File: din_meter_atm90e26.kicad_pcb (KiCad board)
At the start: 2 copper layers, 32 x 31.1 mm, 61 parts, among them J1 USEL, J2 MMD1, J3 MMD0, J4 CONN_02X18, J5 CONN_01X10, J6 USEL, J7 MMD1, J8 MMD0, M1 ATM90E26_ATM90E26, M2 ATM90E26_ATM90E26, Y1 Crystal_Small, Y2 Crystal_Small

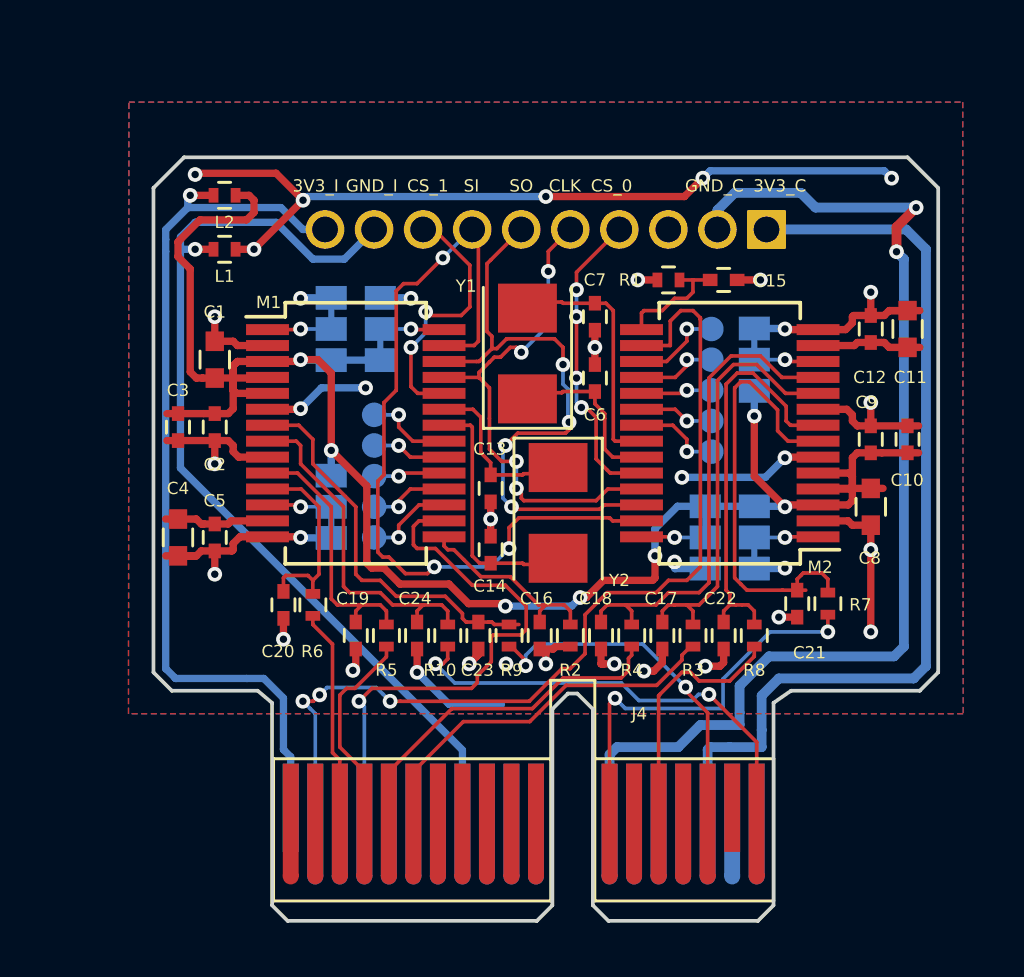
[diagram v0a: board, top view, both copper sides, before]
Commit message: First pass at layout.
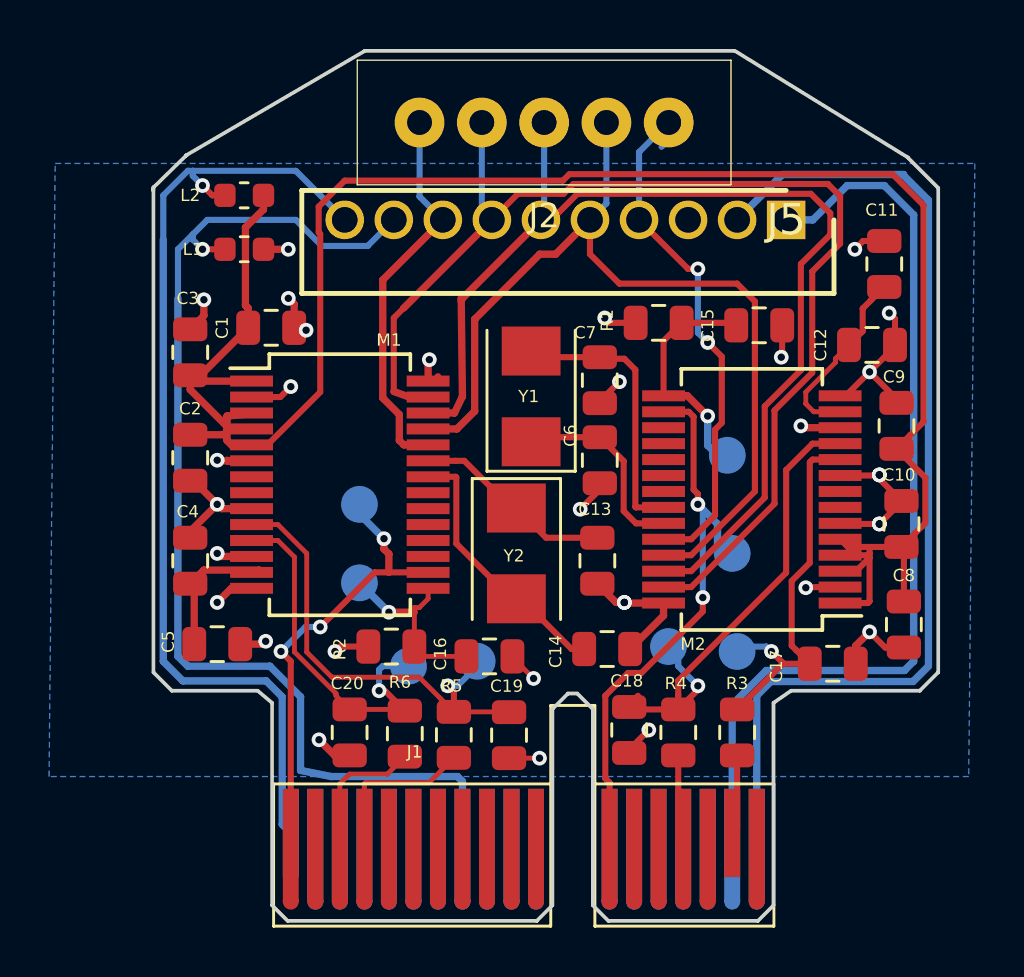
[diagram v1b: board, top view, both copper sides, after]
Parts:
- removed C21, C22, C23, C24: 33n, Capacitors_SMD:C_0402
- removed CF1_0: CF1_0, Measurement_Points:Measurement_Point_Round-SMD-Pad_Small
- removed CF1_1: CF1_1, Measurement_Points:Measurement_Point_Round-SMD-Pad_Small
- removed CF2_0: CF2_0, Measurement_Points:Measurement_Point_Round-SMD-Pad_Small
- removed CF2_1: CF2_1, Measurement_Points:Measurement_Point_Round-SMD-Pad_Small
- removed IRQ_0: IRQ_0, Measurement_Points:Measurement_Point_Round-SMD-Pad_Small
- removed IRQ_1: IRQ_1, Measurement_Points:Measurement_Point_Round-SMD-Pad_Small
- removed J3, J8: MMD0, Connectors:GS3
- removed J4: CONN_02X18, Connectors:PCI-EXPRESS
- removed J6: USEL, Connectors:GS3
- removed J7: MMD1, Connectors:GS3
- removed LOGO1: Logo_Open_Hardware_Small, Symbols:OSHW-Logo2_7.3x6mm_SilkScreen
- removed R10, R7, R8, R9: 1K, Resistors_SMD:R_0402
- removed WARN_0: WARN_0, Measurement_Points:Measurement_Point_Round-SMD-Pad_Small
- removed WARN_1: WARN_1, Measurement_Points:Measurement_Point_Round-SMD-Pad_Small
- removed ZX_0: ZX_0, Measurement_Points:Measurement_Point_Round-SMD-Pad_Small
- removed ZX_1: ZX_1, Measurement_Points:Measurement_Point_Round-SMD-Pad_Small
- added TP_I1N_0: I1N_0, MeasurementPoints:Measurement_Point_Round-SMD-Pad_Small, B.Cu at (150.9, 78.3)
- added TP_I1N_1: I1N_1, MeasurementPoints:Measurement_Point_Round-SMD-Pad_Small, B.Cu at (140.3, 79.2)
- added TP_I1P_0: I1P_0, MeasurementPoints:Measurement_Point_Round-SMD-Pad_Small, B.Cu at (153.7, 78.5)
- added TP_I1P_1: I1P_1, MeasurementPoints:Measurement_Point_Round-SMD-Pad_Small, B.Cu at (143.1, 79.0)
- added TP_VN_0: VN_0, MeasurementPoints:Measurement_Point_Round-SMD-Pad_Small, B.Cu at (153.3, 70.5)
- added TP_VN_1: VN_1, MeasurementPoints:Measurement_Point_Round-SMD-Pad_Small, B.Cu at (138.3, 75.8)
- added TP_VP_0: VP_0, MeasurementPoints:Measurement_Point_Round-SMD-Pad_Small, B.Cu at (153.5, 74.5)
- added TP_VP_1: VP_1, MeasurementPoints:Measurement_Point_Round-SMD-Pad_Small, B.Cu at (138.3, 72.5)
- C1, C11, C4, C8: footprint Capacitors_SMD:C_0603 -> Capacitor_SMD:C_0805_2012Metric
- C10, C12, C2, C3, C5, C9: value 100n -> .1u; footprint Capacitors_SMD:C_0402 -> Capacitor_SMD:C_0805_2012Metric
- C13, C14, C6, C7: footprint Capacitors_SMD:C_0402 -> Capacitor_SMD:C_0805_2012Metric
- C15, C16, C17, C18, C19, C20: value 33n -> .033u; footprint Capacitors_SMD:C_0402 -> Capacitor_SMD:C_0805_2012Metric
- J1: value USEL -> PCIx1; footprint Connectors:GS3 -> Connectors:PCI-EXPRESS; moved to F.Cu
- J2: value MMD1 -> Conn_01x05; footprint Connectors:GS3 -> FitHome_conn:conn_5_2.54mm; moved to F.Cu
- J5: moved to F.Cu
- L1, L2: footprint Inductors_SMD:L_0402 -> Inductor_SMD:L_0603_1608Metric
- M1, M2: footprint Housings_SSOP:SSOP-28_5.3x10.2mm_Pitch0.65mm -> Housings:SSOP-28_5.3x10.2mm_Pitch0.65mm
- R1, R2, R3, R4, R5, R6: footprint Resistors_SMD:R_0402 -> Resistor_SMD:R_0805_2012Metric
- Y1, Y2: footprint Crystals:Crystal_SMD_5032-2pin_5.0x3.2mm -> Crystal:Crystal_SMD_5032-2Pin_5.0x3.2mm
- moved SYM1 19.4 mm to (139.3, 67.0), turned to 180 degrees
- moved G1 16.6 mm to (152.7, 66.9)
- moved J1 13.4 mm to (135.5, 86.0)
- moved J2 9.16 mm to (140.8, 57.0), turned to 0 degrees
- moved C19 7.45 mm to (144.4, 82.0)
- moved R2 7.31 mm to (139.6, 78.3), turned to 180 degrees
- moved C17 7.04 mm to (157.6, 79.0), turned to 180 degrees
- moved R6 6.45 mm to (140.2, 81.9)
- moved C14 6.24 mm to (148.4, 78.5), turned to 180 degrees
- moved C20 5.86 mm to (137.9, 81.8)
- moved C13 5.26 mm to (148.0, 74.8)
- moved C8 4.99 mm to (160.5, 77.5)
- moved R5 4.90 mm to (142.2, 82.0)
- moved R4 4.38 mm to (151.3, 81.8)
- moved C5 4.35 mm to (132.5, 78.2), turned to 0 degrees
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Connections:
- J2 pad 1: GNDD -> CS_1
- J2 pad 2: Net-(J2-Pad2) -> MOSI_M
- J2 pad 3: +3V3 -> MISO_M
- J5 pad 10: 3V3_ISO -> 3V3_M
- J5 pad 5: SCLK -> SCLK_M
- J5 pad 6: SO/TX -> MISO_M
- J5 pad 7: SI/RX -> MOSI_M
- J5 pad 9: GND_ISO -> GND_M
- L1 pad 1: GND_ISO -> GND_M
- L2 pad 1: 3V3_ISO -> 3V3_M
- M1 pad 1: Net-(J2-Pad2) -> +3V3
- M1 pad 12: Net-(J1-Pad2) -> GNDD
- M1 pad 25: SCLK -> SCLK_M
- M1 pad 26: SO/TX -> MISO_M
- M1 pad 27: SI/RX -> MOSI_M
- M1 pad 28: Net-(J3-Pad2) -> GNDD
- M1 pad 7: I2P_1 -> Net-(M1-Pad7)
- M1 pad 8: I2N_1 -> Net-(M1-Pad8)
- M2 pad 1: Net-(J7-Pad2) -> +3V3
- M2 pad 12: Net-(J6-Pad2) -> GNDD
- M2 pad 25: SCLK -> SCLK_M
- M2 pad 26: SO/TX -> MISO_M
- M2 pad 27: SI/RX -> MOSI_M
- M2 pad 28: Net-(J8-Pad2) -> GNDD
- M2 pad 7: I2P_0 -> Net-(M2-Pad7)
- M2 pad 8: I2N_0 -> Net-(M2-Pad8)
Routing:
- net MOSI_M: track 0.00 -> 49.2 mm
- net GNDD: track 106.0 -> 58.0 mm, vias 37 -> 32
- net GND_M: track 0.00 -> 46.4 mm, vias 0 -> 1
- net MISO_M: track 0.00 -> 45.2 mm
- net 3V3_M: track 0.00 -> 40.6 mm, vias 0 -> 1
- net GND_ISO: track 39.2 -> 0.00 mm, vias 1 -> 0
- net SCLK_M: track 0.00 -> 38.0 mm
- net 3V3_ISO: track 36.5 -> 0.00 mm, vias 1 -> 0
- net SI/RX: track 34.2 -> 0.00 mm, vias 3 -> 0
- net SO/TX: track 25.3 -> 0.00 mm, vias 4 -> 0
- net SCLK: track 20.8 -> 0.00 mm, vias 4 -> 0
- net I2N_1_IN: track 18.9 -> 0.00 mm, vias 2 -> 0
- net I2P_0: track 18.3 -> 0.00 mm
- net I2N_0: track 16.7 -> 0.00 mm
- net I2P_0_IN: track 16.6 -> 0.00 mm, vias 2 -> 0
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- removed copper zone on F.Cu, net GNDD
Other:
- board size 32 x 31.1 mm -> 32 x 35.5 mm
- board text added: "Thanks to"
- board text removed: "3V3_C"
- board text removed: "3V3_I"
- board text removed: "CLK"
- board text removed: "CS_0"
- board text removed: "CS_1"
- board text removed: "Dual ATM90E26 Metering v1.3 22/01/2018 OSHW TAPR"
- board text removed: "GND_C"
- board text removed: "GND_I"
- board text removed: "SI"
- board text removed: "SO"
